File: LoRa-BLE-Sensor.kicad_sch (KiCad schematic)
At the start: 118 parts, among them J1 SHF-105-01-X-D-SM, J2 Battery_Cell, J3 Conn_01x06_Socket, J4 Screw_Terminal_01x04, J5 Screw_Terminal_01x06, J6 Screw_Terminal_01x06, J7 Conn_01x10_Pin, Q1 DMN67D7L, Q10 SQ2389ES, Q11 DMN62D0UDW-7, Q12 DMN62D0UDW-7, Q13 SQ2389ES, Q2 DMN67D7L, Q3 DMN67D7L, Q4 DMN67D7L, Q5 DMN67D7L, Q6 DMN67D7L, Q7 DMN67D7L, Q8 DMN67D7L, Q9 SQ2389ES, SW1 SW_Push, SW2 SW_Push, SW3 SW_Push, U1 RAK4630, U2 NPM1300-QEAA-R, U3 TLV61046ADBVR, U4 TLV61046ADBVR, U5 TLV61046ADBVR

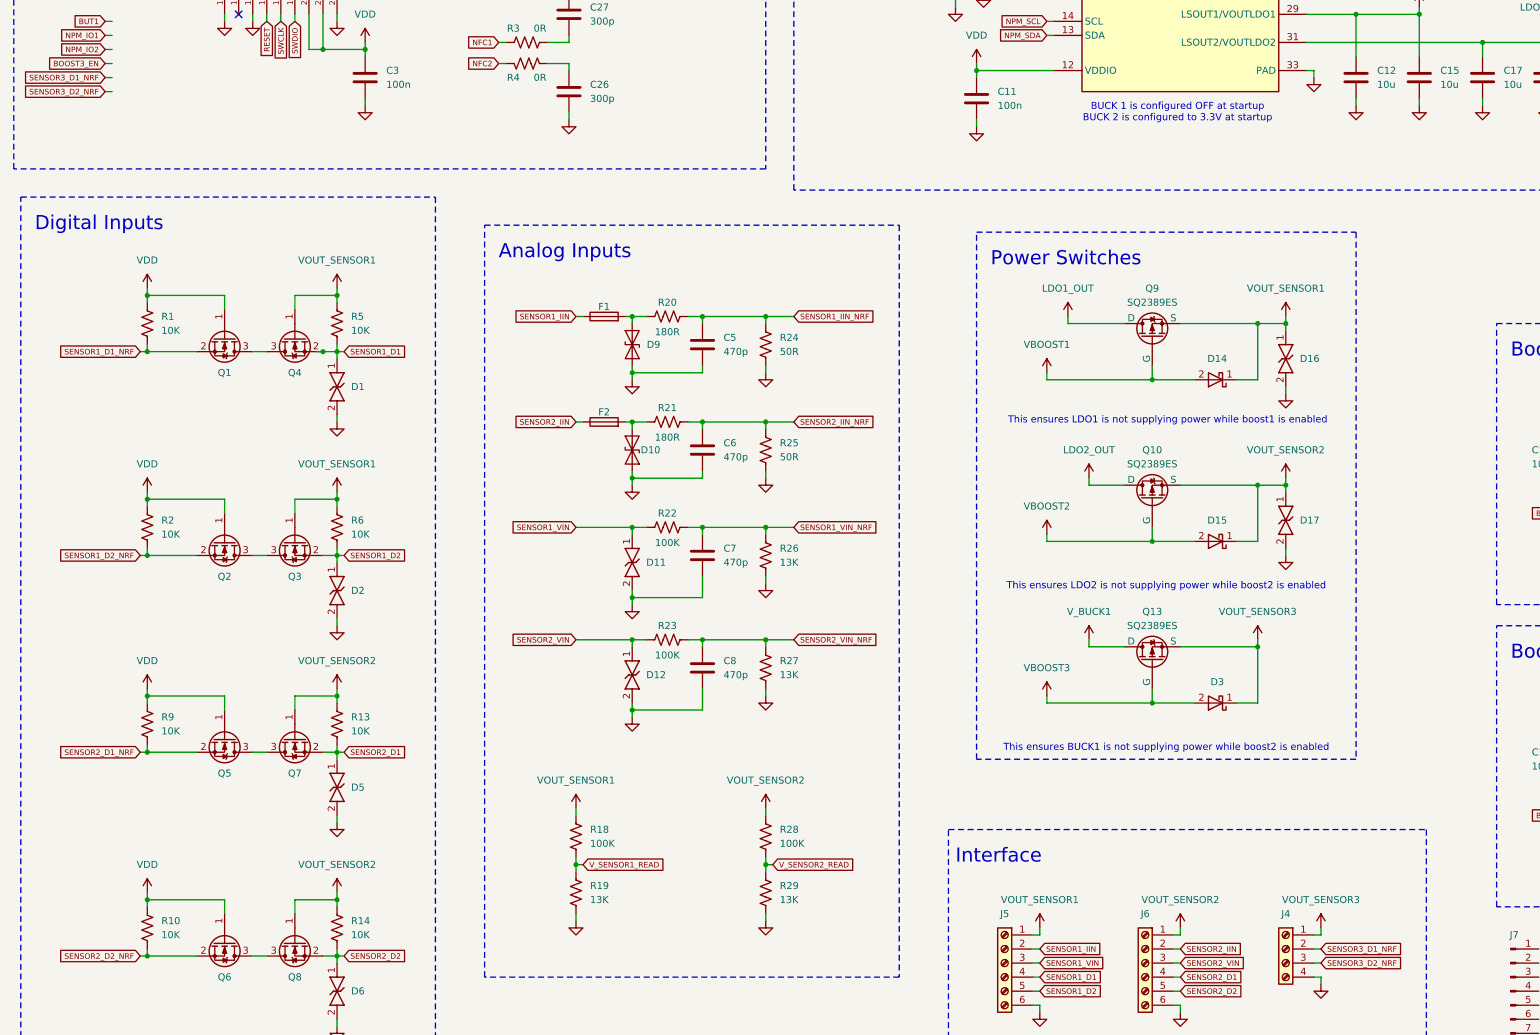
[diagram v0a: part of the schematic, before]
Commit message: sensor3 schematic almost done
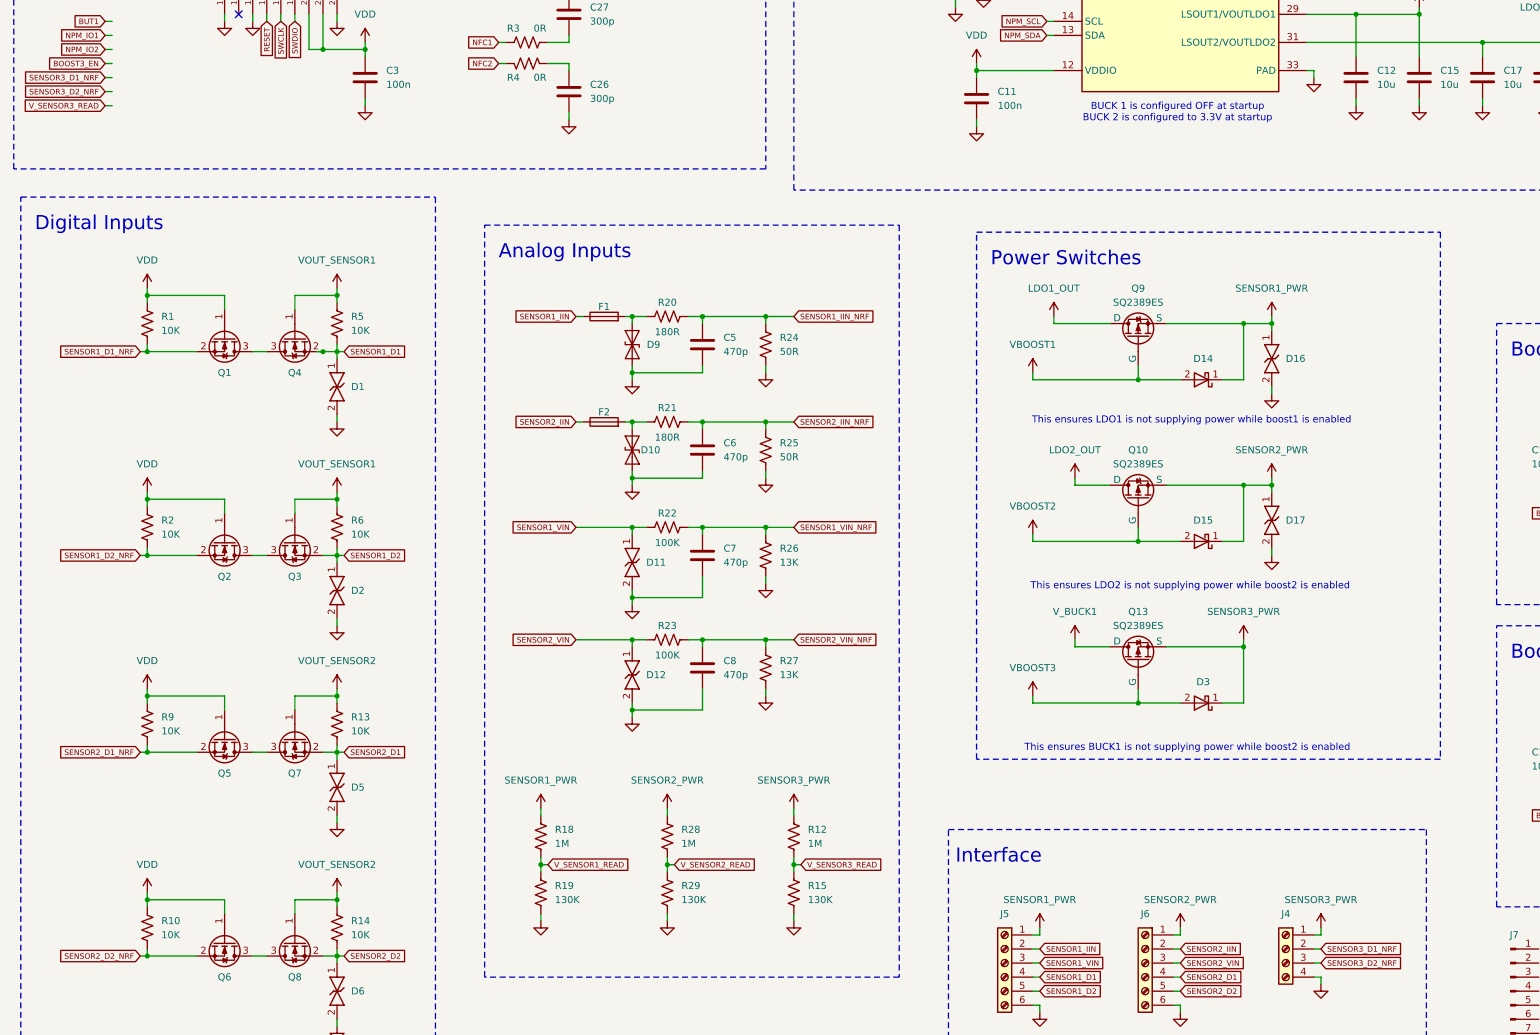
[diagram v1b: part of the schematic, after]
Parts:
- added R12: 1M, Resistor_SMD:R_0402_1005Metric, symbol Device:R_US
- added R15: 130K, Resistor_SMD:R_0402_1005Metric, symbol Device:R_US
- R18, R28: value 100K -> 1M
- R19, R29: value 13K -> 130K
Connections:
- net GND: now also R15.2
- net VOUT_SENSOR1: no longer D14.1 (K), D16.1, J5.1 (Pin_1), Q9.2 (S), R18.1
- net VOUT_SENSOR2: no longer D15.1 (K), D17.1, J6.1 (Pin_1), Q10.2 (S), R28.1
- net VOUT_SENSOR3: no longer D3.1 (K), J4.1 (Pin_1), Q13.2 (S)
- new net SENSOR1_PWR: D14.1 (K), D16.1, J5.1 (Pin_1), Q9.2 (S), R18.1
- new net SENSOR2_PWR: D15.1 (K), D17.1, J6.1 (Pin_1), Q10.2 (S), R28.1
- new net SENSOR3_PWR: D3.1 (K), J4.1 (Pin_1), Q13.2 (S), R12.1
- new net V_SENSOR3_READ: R12.2, R15.1
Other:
- moved on the sheet: D14, D15, D16, D17, D3, Q10, Q13, Q9, R18, R19, R28, R29

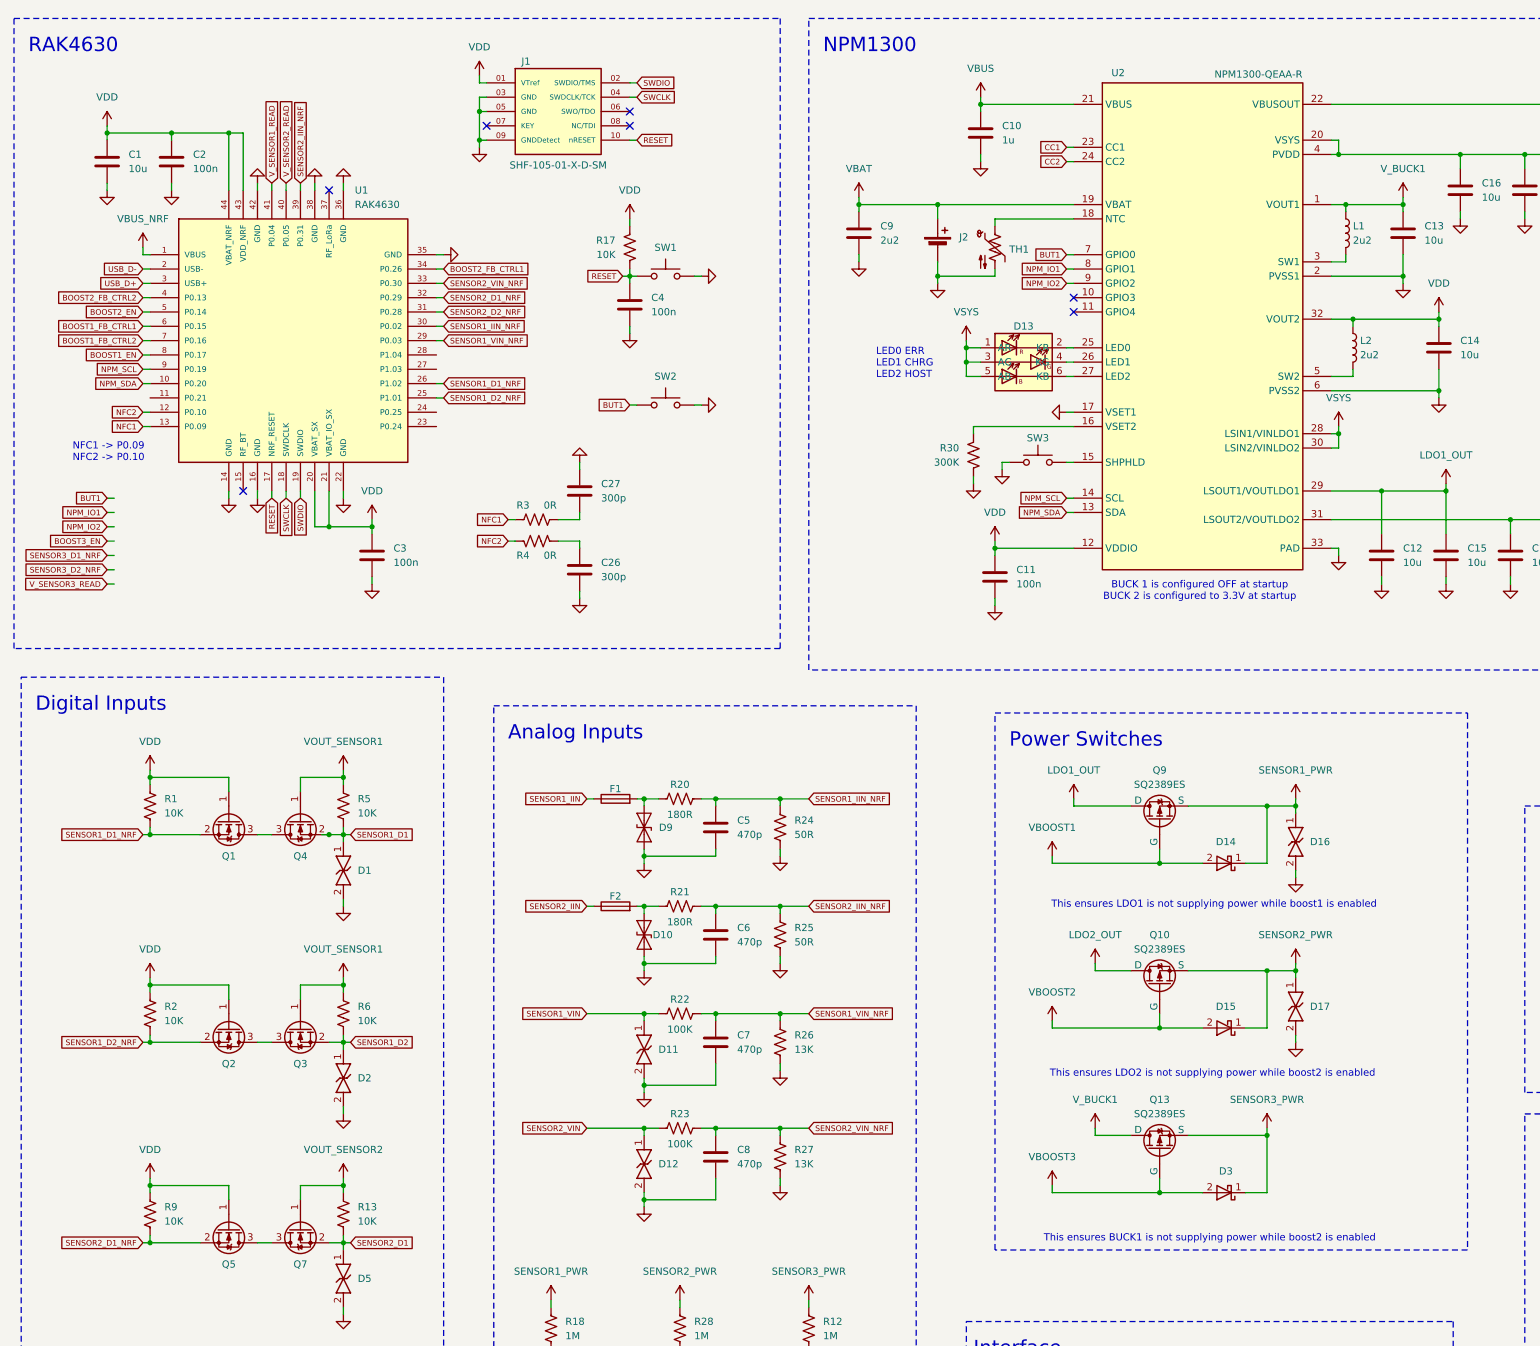
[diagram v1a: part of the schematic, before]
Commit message: Beginning routing V1.1
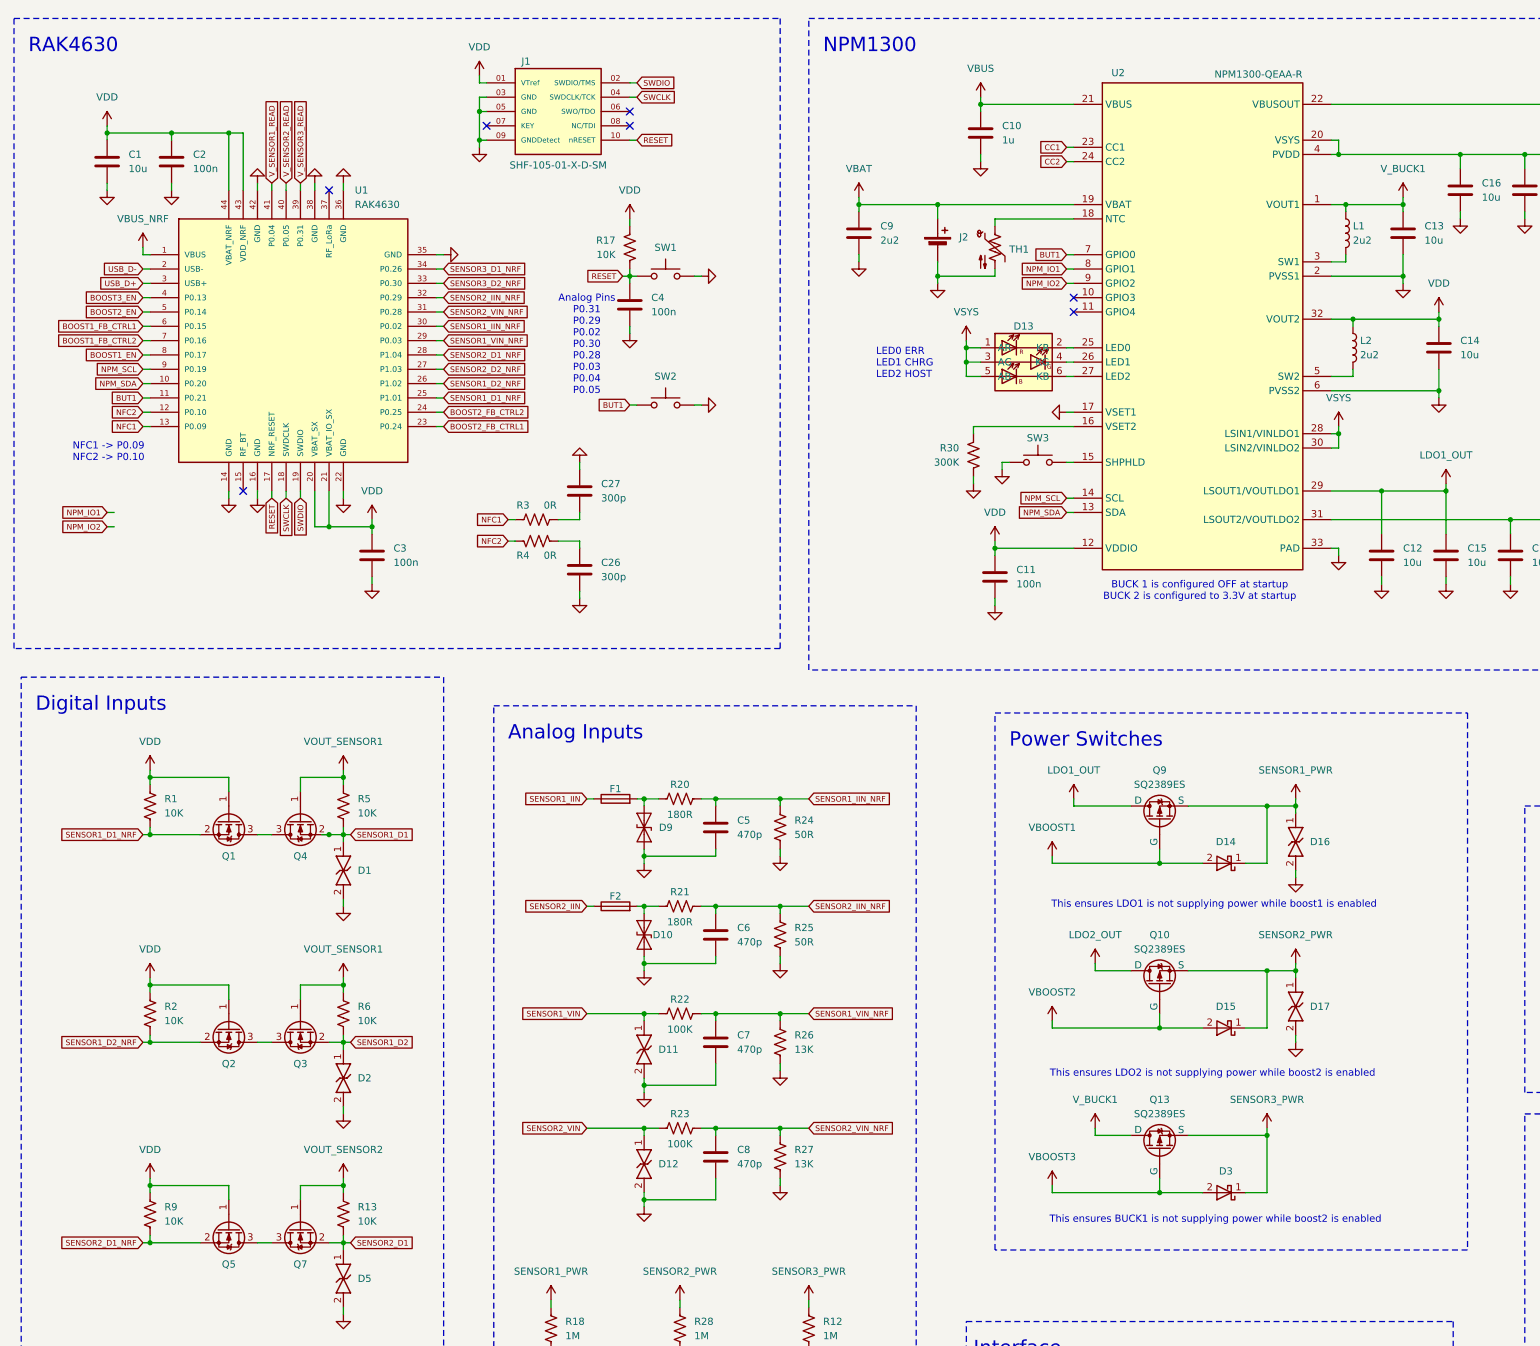
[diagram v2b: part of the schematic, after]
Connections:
- net BOOST2_FB_CTRL1: now also U1.23 (P0.24); no longer U1.34 (P0.26)
- net BOOST2_FB_CTRL2: now also U1.24 (P0.25); no longer U1.4 (P0.13)
- net BOOST3_EN: now also U1.4 (P0.13)
- net BUT1: now also U1.11 (P0.21)
- net SENSOR1_D1_NRF: now also U1.25 (P1.01); no longer U1.26 (P1.02)
- net SENSOR1_D2_NRF: now also U1.26 (P1.02); no longer U1.25 (P1.01)
- net SENSOR2_D1_NRF: now also U1.28 (P1.04); no longer U1.32 (P0.29)
- net SENSOR2_D2_NRF: now also U1.27 (P1.03); no longer U1.31 (P0.28)
- net SENSOR2_IIN_NRF: now also U1.32 (P0.29); no longer U1.39 (P0.31)
- net SENSOR2_VIN_NRF: now also U1.31 (P0.28); no longer U1.33 (P0.30)
- net SENSOR3_D1_NRF: now also U1.34 (P0.26)
- net SENSOR3_D2_NRF: now also U1.33 (P0.30)
- net V_SENSOR3_READ: now also U1.39 (P0.31)
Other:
- note added: "Analog Pins P0.31 P0.29 P0.02 P0.30 P0.28 P0.03 P0.04 P0.05"

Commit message: signal routing
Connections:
- net BOOST1_FB_CTRL1: now also U1.23 (P0.24); no longer U1.6 (P0.15)
- net BOOST1_FB_CTRL2: now also U1.24 (P0.25); no longer U1.7 (P0.16)
- net BOOST2_FB_CTRL1: now also U1.6 (P0.15); no longer U1.23 (P0.24)
- net BOOST2_FB_CTRL2: now also U1.7 (P0.16); no longer U1.24 (P0.25)
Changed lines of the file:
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@@
 	(wire
 		(pts
+			(xy 92.71 87.63) (xy 93.98 87.63)
+		)
+		(stroke
+			(width 0)
+			(type default)
+		)
+	)
+	(wire
+		(pts
 			(xy 92.71 72.39) (xy 93.98 72.39)
 		)
@@
 	(wire
 		(pts
-			(xy 93.98 90.17) (xy 92.71 90.17)
-		)
-		(stroke
-			(width 0)
-			(type default)
-		)
-	)
-	(wire
-		(pts
 			(xy 340.36 179.07) (xy 354.33 179.07)
 		)
@@
 	(wire
 		(pts
+			(xy 93.98 90.17) (xy 92.71 90.17)
+		)
+		(stroke
+			(width 0)
+			(type default)
+		)
+	)
+	(wire
+		(pts
 			(xy 387.35 134.62) (xy 392.43 134.62)
 		)
@@
 	(wire
 		(pts
+			(xy 40.64 72.39) (xy 41.91 72.39)
+		)
+		(stroke
+			(width 0)
+			(type default)
+		)
+	)
+	(wire
+		(pts
 			(xy 40.64 69.85) (xy 41.91 69.85)
 		)
@@
 	(wire
 		(pts
-			(xy 40.64 72.39) (xy 41.91 72.39)
-		)
-		(stroke
-			(width 0)
-			(type default)
-		)
-	)
-	(wire
-		(pts
 			(xy 378.46 259.08) (xy 377.19 259.08)
 		)
@@
 	(wire
 		(pts
-			(xy 92.71 87.63) (xy 93.98 87.63)
-		)
-		(stroke
-			(width 0)
-			(type default)
-		)
-	)
-	(wire
-		(pts
 			(xy 129.54 166.37) (xy 129.54 167.64)
 		)
@@
 		)
 	)
+	(global_label "BOOST1_FB_CTRL2"
+		(shape input)
+		(at 93.98 87.63 0)
+		(fields_autoplaced yes)
+		(effects
+			(font
+				(size 1 1)
+			)
+			(justify left)
+		)
+		(property "Intersheetrefs" "${INTERSHEET_REFS}"
+			(at 109.9969 87.63 0)
+			(effects
+				(font
+					(size 1.27 1.27)
+				)
+				(justify left)
+				(hide yes)
+			)
+		)
+	)
 	(global_label "NPM_IO1"
 		(shape input)
@@
 		)
 	)
-	(global_label "SENSOR1_D1_NRF"
+	(global_label "BOOST2_FB_CTRL1"
 		(shape input)
-		(at 93.98 85.09 0)
+		(at 40.64 72.39 180)
 		(fields_autoplaced yes)
 		(effects
@@
 				(size 1 1)
 			)
-			(justify left)
+			(justify right)
 		)
 		(property "Intersheetrefs" "${INTERSHEET_REFS}"
-			(at 109.5684 85.09 0)
+			(at 24.6231 72.39 0)
 			(effects
 				(font
 					(size 1.27 1.27)
 				)
-				(justify left)
+				(justify right)
 				(hide yes)
 			)
 		)
 	)
-	(global_label "BOOST2_FB_CTRL2"
+	(global_label "SENSOR1_D1_NRF"
 		(shape input)
-		(at 93.98 87.63 0)
+		(at 93.98 85.09 0)
 		(fields_autoplaced yes)
 		(effects
@@
 		)
 		(property "Intersheetrefs" "${INTERSHEET_REFS}"
-			(at 109.9969 87.63 0)
+			(at 109.5684 85.09 0)
 			(effects
 				(font
@@
 	(global_label "BOOST2_FB_CTRL2"
 		(shape input)
+		(at 40.64 74.93 180)
+		(fields_autoplaced yes)
+		(effects
+			(font
+				(size 1 1)
+			)
+			(justify right)
+		)
+		(property "Intersheetrefs" "${INTERSHEET_REFS}"
+			(at 24.6231 74.93 0)
+			(effects
+				(font
+					(size 1.27 1.27)
+				)
+				(justify right)
+				(hide yes)
+			)
+		)
+	)
+	(global_label "BOOST2_FB_CTRL2"
+		(shape input)
 		(at 393.7 250.19 0)
 		(fields_autoplaced yes)
@@
 		)
 	)
-	(global_label "BOOST1_FB_CTRL1"
-		(shape input)
-		(at 40.64 72.39 180)
-		(fields_autoplaced yes)
-		(effects
-			(font
-				(size 1 1)
-			)
-			(justify right)
-		)
-		(property "Intersheetrefs" "${INTERSHEET_REFS}"
-			(at 24.6231 72.39 0)
-			(effects
-				(font
-					(size 1.27 1.27)
-				)
-				(justify right)
-				(hide yes)
-			)
-		)
-	)
 	(global_label "BOOST2_EN"
 		(shape input)
@@
 		)
 	)
-	(global_label "BOOST1_FB_CTRL2"
-		(shape input)
-		(at 40.64 74.93 180)
-		(fields_autoplaced yes)
-		(effects
-			(font
-				(size 1 1)
-			)
-			(justify right)
-		)
-		(property "Intersheetrefs" "${INTERSHEET_REFS}"
-			(at 24.6231 74.93 0)
-			(effects
-				(font
-					(size 1.27 1.27)
-				)
-				(justify right)
-				(hide yes)
-			)
-		)
-	)
 	(global_label "NPM_SDA"
 		(shape input)
@@
 		)
 	)
-	(global_label "BOOST2_FB_CTRL1"
+	(global_label "BOOST1_FB_CTRL1"
 		(shape input)
 		(at 93.98 90.17 0)
